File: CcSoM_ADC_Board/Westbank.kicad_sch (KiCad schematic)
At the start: 1 part, among them J1 SoM Connector

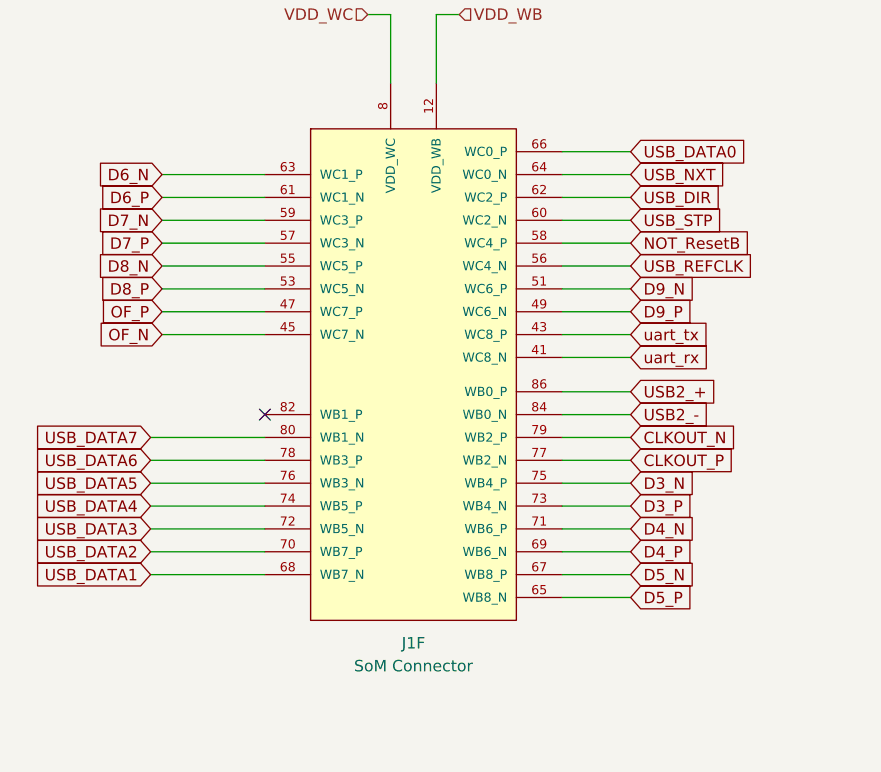
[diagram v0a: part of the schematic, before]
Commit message: changed from 10Bit ADC to 12Bit
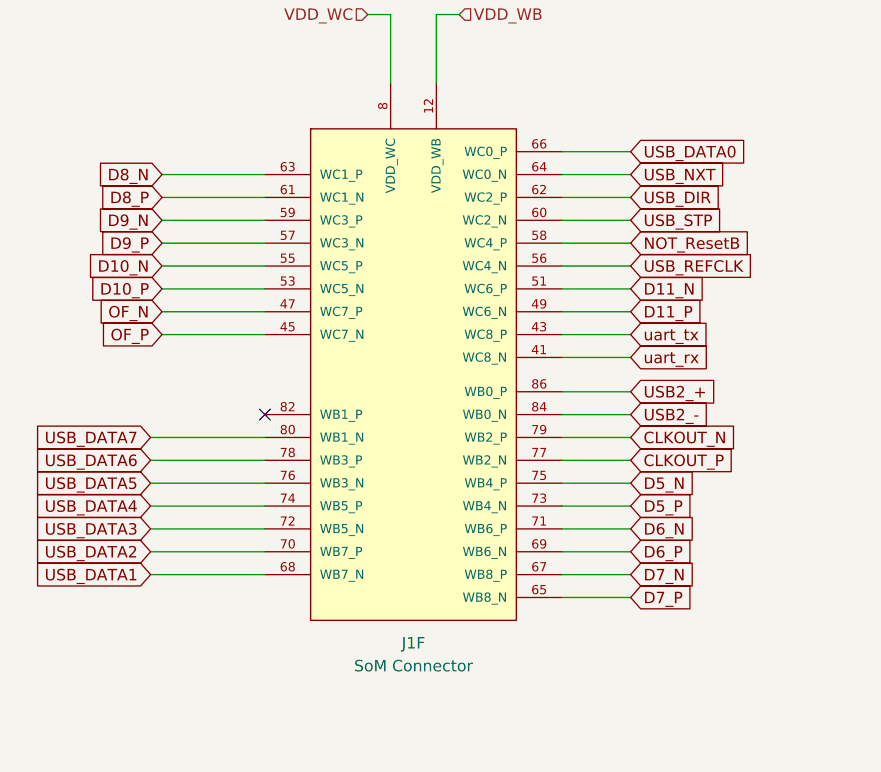
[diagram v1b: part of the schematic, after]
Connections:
- net D3_N is gone; now on net D5_N: J1.75 (WB4_P)
- net D3_P is gone; now on net D5_P: J1.73 (WB4_N)
- net D4_N is gone; now on net D6_N: J1.71 (WB6_P)
- net D4_P is gone; now on net D6_P: J1.69 (WB6_N)
- net D5_N: no longer J1.67 (WB8_P)
- net D5_P: no longer J1.65 (WB8_N)
- net D6_N: no longer J1.63 (WC1_P)
- net D6_P: no longer J1.61 (WC1_N)
- net D7_N: now also J1.67 (WB8_P); no longer J1.59 (WC3_P)
- net D7_P: now also J1.65 (WB8_N); no longer J1.57 (WC3_N)
- net D8_N: now also J1.63 (WC1_P); no longer J1.55 (WC5_P)
- net D8_P: now also J1.61 (WC1_N); no longer J1.53 (WC5_N)
- net D9_N: now also J1.59 (WC3_P); no longer J1.51 (WC6_P)
- net D9_P: now also J1.57 (WC3_N); no longer J1.49 (WC6_N)
- net OF_N: now also J1.47 (WC7_P); no longer J1.45 (WC7_N)
- net OF_P: now also J1.45 (WC7_N); no longer J1.47 (WC7_P)
- new net D10_N: J1.55 (WC5_P)
- new net D10_P: J1.53 (WC5_N)
- new net D11_N: J1.51 (WC6_P)
- new net D11_P: J1.49 (WC6_N)

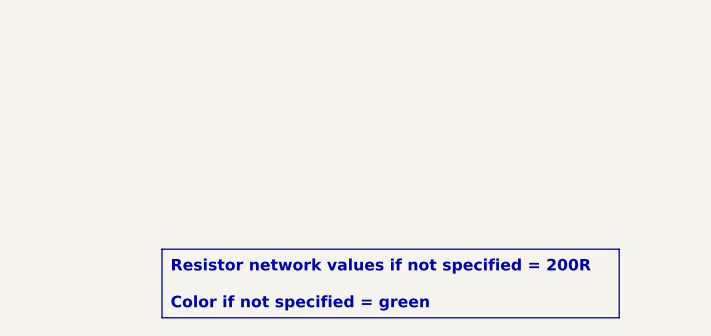
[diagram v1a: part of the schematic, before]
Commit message: corrected schematic created pdf and bom file
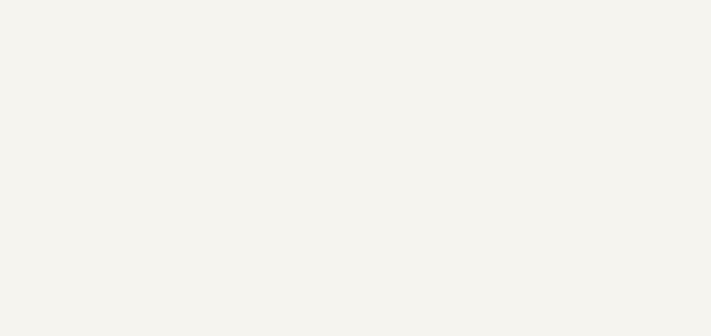
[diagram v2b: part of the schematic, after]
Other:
- title: SoM Programmer & Tester -> SoM Programmer & ADC Board
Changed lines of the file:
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@@
 	(paper "A4")
 	(title_block
-		(title "SoM Programmer & Tester")
+		(title "SoM Programmer & ADC Board")
 		(date "2024-12-20")
 		(rev "0.1")
 		(company "Technische Hochschule Köln")
 		(comment 1 "Felix Sebastian Nitz")
-	)
-	(text_box "Resistor network values if not specified = 200R\n\nColor if not specified = green"
-		(exclude_from_sim no)
-		(at 228.6 152.4 0)
-		(size 50.8 7.62)
-		(margins 0.9525 0.9525 0.9525 0.9525)
-		(stroke
-			(width 0)
-			(type default)
-		)
-		(fill
-			(type none)
-		)
-		(effects
-			(font
-				(size 1.27 1.27)
-				(thickness 0.254)
-				(bold yes)
-			)
-			(justify left)
-		)
+		(comment 2 "Ismail Özdemirkan")
 	)
 	(no_connect

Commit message: digikey no not complete
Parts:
- J1: DigiKey_no (none) -> A121565-ND
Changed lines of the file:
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@@
+			)
+		)
+		(property "DigiKey_no" "A121565-ND"
+			(at 130.81 83.82 0)
+			(effects
+				(font
+					(size 1.27 1.27)
+				)
+				(hide yes)
 			)
 		)
